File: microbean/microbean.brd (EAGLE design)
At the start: 30.5 x 27.6 mm, 17 parts, among them IC2 MAX485ST3485, IC3 PIC16F1827SO

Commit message: - WIP microbean for professional printing
git-svn-id: svn://mule/net/hardware/trunk@556 1a6b750e-079f-425f-90e7-3a118970be6b
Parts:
- added J5: (no value), custom:1X02
- added U$4: (no value), holes:2,8
- moved C5 5.24 mm to (11.4, 27.9), flipped to the bottom, turned to 0 degrees
- moved IC2 3.59 mm to (19.1, 26.7), flipped to the top, turned to 90 degrees
- moved C2 2.84 mm to (26.7, 26.7), flipped to the top, turned to 90 degrees
- moved J1 2.54 mm to (3.81, 26.7)
- moved J2 2.54 mm to (3.81, 19.1)
- moved C1 1.80 mm to (11.4, 30.5), flipped to the bottom, turned to 180 degrees
- moved D3 1.27 mm to (6.35, 35.6)
- moved C3 1.27 mm to (10.2, 35.6)
- moved J4 1.27 mm to (20.3, 14.0)
- moved U$2 1.27 mm to (27.9, 15.2)
- turned C4 to 270 degrees
- turned IC1 to 180 degrees
- flipped IC3 to the bottom
- turned R1 to 180 degrees
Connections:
- net GND: now also J5.2
- net N$10: now also R1.2; no longer R1.1
- net N$13: now also J5.1
- net N$14: now also IC3.7; no longer IC3.1
- net N$15: now also IC3.6; no longer IC3.2
- net N$17: now also IC3.2; no longer IC3.6
- net N$18: now also IC3.1; no longer IC3.7
- net N$19: now also IC3.17; no longer IC3.9
- net N$20: now also IC3.16; no longer IC3.10
- net N$21: now also IC3.10; no longer IC3.15
- net N$4: now also IC3.15; no longer IC3.16
- net N$9: now also IC3.9, R1.1; no longer IC3.17, R1.2
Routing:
- net GND: track 0.00 -> 103.6 mm
- net N$13: track 0.00 -> 79.3 mm, vias 0 -> 1
- net N$23: track 0.00 -> 21.7 mm, vias 0 -> 1
- net N$6: track 0.00 -> 18.7 mm
- net N$18: track 0.00 -> 18.2 mm
- net N$3: track 0.00 -> 15.2 mm
- net N$5: track 0.00 -> 14.1 mm
- net N$8: track 0.00 -> 14.0 mm
- net N$2: track 0.00 -> 12.9 mm, vias 0 -> 1
- net N$9: track 0.00 -> 12.5 mm, vias 0 -> 1
- net N$16: track 0.00 -> 11.9 mm
- net N$7: track 0.00 -> 11.4 mm
- net N$14: track 0.00 -> 11.1 mm
- net N$15: track 0.00 -> 10.7 mm
- net N$17: track 0.00 -> 10.5 mm
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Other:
- board size 30.5 x 27.6 mm -> 33 x 27.6 mm

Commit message: - WIP, DRU finished
git-svn-id: svn://mule/net/hardware/trunk@557 1a6b750e-079f-425f-90e7-3a118970be6b
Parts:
- moved C5 1.91 mm to (13.3, 27.9)
- renumbered U$1 to ICSP, U$3 to D2
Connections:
- net N$13 renamed VCC
- net N$14 renamed RB1
- net N$15 renamed RB0
- net N$16 renamed RA4
- net N$17 renamed RA3
- net N$18 renamed RA2
- net N$19 renamed RA0
- net N$20 renamed RA7
- net N$21 renamed RB4
- net N$3 renamed B
- net N$4 renamed RA6
- net N$5 renamed A
- net N$6 renamed MCLR
- net N$7 renamed DAT
- net N$8 renamed CLK
- net GND: now also IC1.2@1
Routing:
- net N$23: track 21.7 -> 9.31 mm
- net VCC: track 79.3 -> 88.7 mm, vias 1 -> 2
- net CLK: track 14.0 -> 17.5 mm, vias 0 -> 1
- net RA2: track 18.2 -> 21.6 mm
- net RA4: track 11.9 -> 15.1 mm
- net DAT: track 11.4 -> 14.2 mm
- net N$11: track 4.64 -> 5.64 mm
- net GND: track 103.6 -> 102.7 mm, vias 0 -> 1
- net RB1: track 11.1 -> 12.0 mm
- net RB0: track 10.7 -> 11.6 mm
- net N$10: track 2.98 -> 3.49 mm
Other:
- board text added: "+"
- board text added: "-"
- board text added: "A"
- board text added: "A0"
- board text added: "A2"
- board text added: "A3"
- board text added: "A4"
- board text added: "A6"
- board text added: "A7"
- board text added: "B"
- board text added: "B0"
- board text added: "B1"
- board text added: "B4"
- board text added: "BOT"
- board text added: "GND"
- board text added: "ICSP:1"
- board text added: "LUCKYSW 2017-uBEAN"
- board text added: "TOP"
- board text added: "VCC"

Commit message: - Refinements
git-svn-id: svn://mule/net/hardware/trunk@560 1a6b750e-079f-425f-90e7-3a118970be6b
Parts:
- C1, C2, C5: value (none) -> 100n
- C3, C4: value (none) -> 10u
- D3: value S1M -> S1A
- IC1: value (none) -> L78L33/L78L05
- IC2: value MAX485ST3485 -> ST485/ST3485
- R1: value (none) -> 560

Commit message: - Finishing up for quoting
git-svn-id: svn://mule/net/hardware/trunk@564 1a6b750e-079f-425f-90e7-3a118970be6b
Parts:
- added J6: (no value), custom:1X02
- IC3: value PIC16F1827SO -> PIC16F1827SO18; device custom:SO-18W -> custom:SO18W
- moved R1 2.84 mm to (6.35, 16.5), flipped to the bottom, turned to 270 degrees
- moved J3 1.27 mm to (21.6, 36.8)
- moved IC3 0.64 mm to (22.9, 26.0)
- moved J5 0.64 mm to (20.3, 15.9)
- moved J4 0.63 mm to (20.3, 13.3)
- flipped D2 to the top, turned to 270 degrees
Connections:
- net N$11 renamed RB5
- net N$12 renamed RB2
- removed net CLK: IC3.12, ICSP.5
- removed net DAT: IC3.13, ICSP.4
- removed net RA6: IC3.15, J3.2
- removed net RA7: IC3.16, J3.3
- new net RA1: IC3.18, J3.2
- new net RB3: IC3.9, J3.4
- new net RB6: IC3.12, ICSP.5, J6.2
- new net RB7: IC3.13, ICSP.4, J6.1
- net N$23: now also IC3.15; no longer IC3.18
- net N$9: now also IC3.16; no longer IC3.9
- net RA0: now also J3.3; no longer J3.4
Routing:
- net RB7: track 0.00 -> 58.9 mm, vias 0 -> 2
- net RB0: track 11.6 -> 52.7 mm, vias 0 -> 1
- net RB6: track 0.00 -> 32.6 mm, vias 0 -> 1
- net RB3: track 0.00 -> 22.3 mm
- net CLK: track 17.5 -> 0.00 mm, vias 1 -> 0
- net DAT: track 14.2 -> 0.00 mm
- net N$9: track 12.7 -> 26.3 mm, vias 1 -> 0
- net RA4: track 15.1 -> 23.1 mm
- net RA1: track 0.00 -> 7.73 mm, vias 0 -> 1
- net RA7: track 4.72 -> 0.00 mm
- net RA6: track 4.14 -> 0.00 mm
- net RA2: track 21.6 -> 25.4 mm, vias 0 -> 2
- net RB1: track 12.0 -> 15.1 mm
- net N$23: track 9.31 -> 6.50 mm
- net VCC: track 88.7 -> 86.0 mm
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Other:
- board text added: "A1"
- board text added: "B3"
- board text added: "B6"
- board text added: "B7"
- board text removed: "A6"
- board text removed: "A7"

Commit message: - Ready for printing, optimized
git-svn-id: svn://mule/net/hardware/trunk@565 1a6b750e-079f-425f-90e7-3a118970be6b
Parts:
- added J7: (no value), custom:1X02
- J3: device custom:1X05 -> custom:1X03
- moved J6 26.2 mm to (29.2, 36.2)
- moved R1 25.5 mm to (27.3, 31.1), flipped to the top
- moved D2 22.6 mm to (21.6, 31.8), turned to 90 degrees
- moved U$4 8.03 mm to (8.89, 14.0)
- moved J1 4.02 mm to (7.62, 27.9)
- moved J2 4.02 mm to (7.62, 20.3)
- moved C5 3.86 mm to (14.0, 24.1), turned to 90 degrees
- moved IC2 2.84 mm to (20.3, 24.1)
- moved C2 1.94 mm to (28.3, 25.6), turned to 270 degrees
- moved C3 1.93 mm to (12.1, 35.2)
- moved D3 1.83 mm to (8.18, 35.6)
- moved C1 1.80 mm to (12.7, 29.2)
- moved IC1 1.43 mm to (15.2, 34.1)
- moved J4 1.31 mm to (21.6, 13.0)
- moved J5 1.28 mm to (21.6, 15.7)
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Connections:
- net N$23 renamed RA6
- net N$9 renamed RA7
- net RA0: now also J3.2; no longer J3.3
- net RA1: now also J3.3; no longer J3.2
- net RA2: now also J4.1; no longer J3.5
- net RA3: now also J4.2; no longer J4.1
- net RA4: now also J4.3; no longer J4.2
- net RB0: now also J4.4; no longer J4.3
- net RB1: now also J7.2; no longer J4.4
- net RB3: now also J7.1; no longer J3.4
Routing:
- net RB7: track 58.9 -> 20.3 mm, vias 2 -> 1
- net RB0: track 52.7 -> 19.6 mm, vias 1 -> 0
- net VCC: track 86.0 -> 60.0 mm, vias 2 -> 3
- net RA7: track 26.3 -> 3.80 mm, vias 0 -> 1
- net RB3: track 22.3 -> 5.62 mm
- net GND: track 103.7 -> 89.7 mm
- net RA2: track 25.4 -> 11.5 mm, vias 2 -> 1
- net RB1: track 15.1 -> 6.33 mm
- net RB6: track 32.6 -> 25.5 mm, vias 1 -> 0
- net B: track 16.8 -> 10.9 mm
- net RA4: track 23.1 -> 28.1 mm
- net RA3: track 11.5 -> 16.1 mm
- net A: track 14.6 -> 10.1 mm
- net RB5: track 4.60 -> 8.05 mm
- net N$2: track 13.4 -> 15.2 mm
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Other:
- board size 33 x 27.6 mm -> 29.9 x 28.4 mm

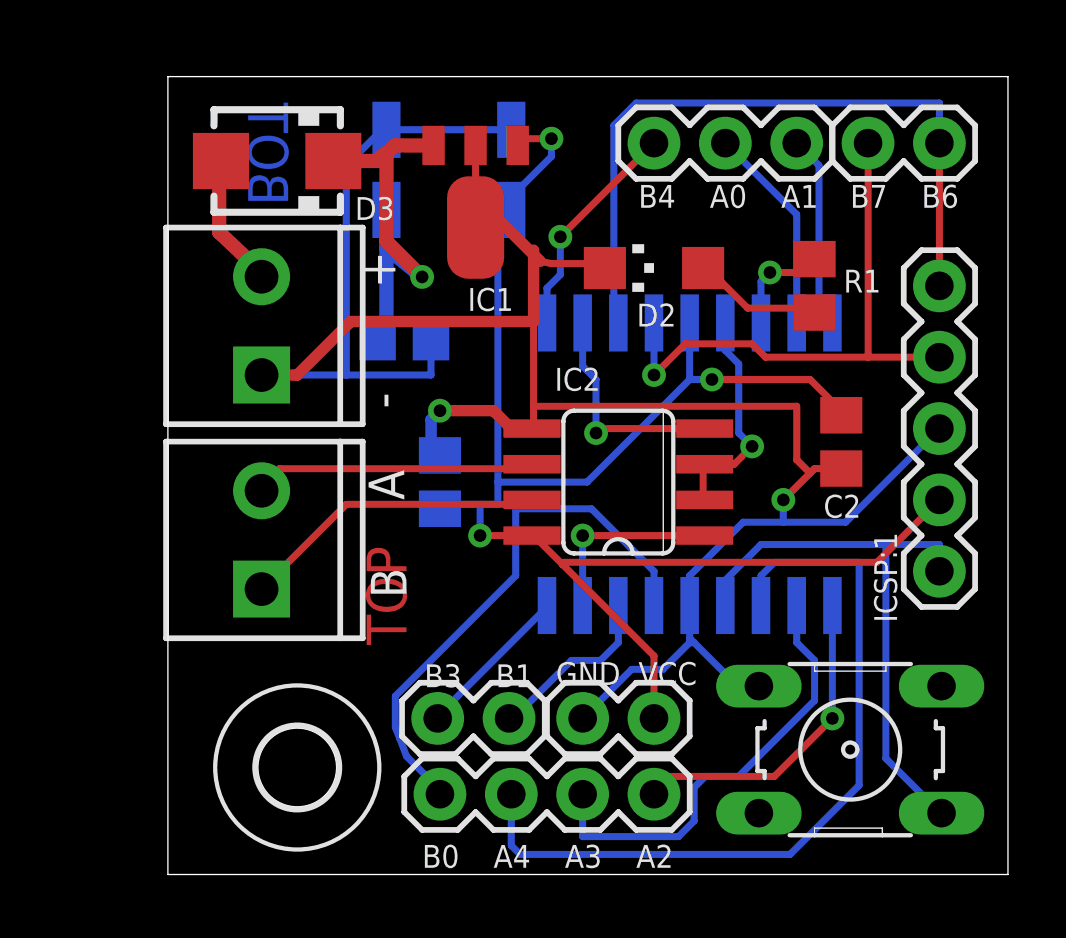
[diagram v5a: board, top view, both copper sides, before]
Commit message: - Fixed via size to comply with drill level A
git-svn-id: svn://mule/net/hardware/trunk@576 1a6b750e-079f-425f-90e7-3a118970be6b
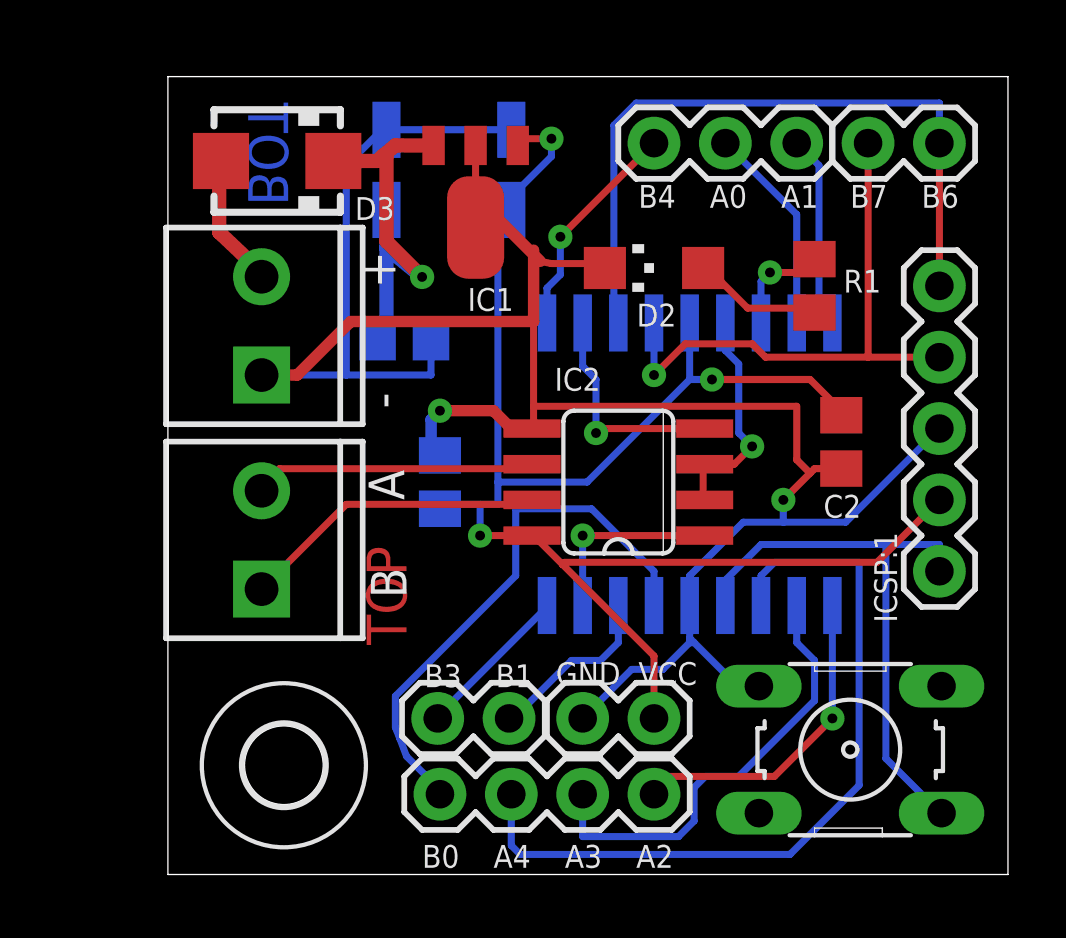
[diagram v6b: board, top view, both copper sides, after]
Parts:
- moved U$4 0.48 mm to (8.41, 14.0)
